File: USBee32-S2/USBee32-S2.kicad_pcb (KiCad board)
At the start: 4 copper layers, 28.1 x 68.3 mm, 50 parts, among them IC1 IP4220CZ6, J1 USB_A, J2 TYPE-C-31-M-12, J3 Conn_01x18_Male, J4 B2B-PH-SM4-TB(LF)(SN), J5 Conn_01x22_Male, Q1 MMBT8050, Q2 MMBT8050, SW1 SW_Push, SW2 SW_Push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

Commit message: Routing and placement cleaned
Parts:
- moved J4 15.1 mm to (171.5, 108.2), turned to 90 degrees
- moved R9 14.0 mm to (172.5, 97.7)
- moved R6 13.2 mm to (180.9, 114.2), turned to 0 degrees
- moved R8 13.0 mm to (172.5, 101.0), turned to 90 degrees
- moved SW2 12.6 mm to (169.2, 118.1)
- moved SW1 11.8 mm to (169.2, 122.0)
- moved C5 11.4 mm to (168.6, 113.6)
- moved C4 11.1 mm to (168.6, 115.4), turned to 0 degrees
- moved C1 10.2 mm to (179.1, 94.1), turned to 90 degrees
- moved R5 9.83 mm to (189.1, 102.7)
- moved Q2 9.75 mm to (186.1, 102.6)
- moved R7 9.23 mm to (175.7, 106.0), turned to 90 degrees
- moved R4 8.17 mm to (189.1, 98.8), turned to 90 degrees
- moved Q1 7.92 mm to (186.1, 98.8)
- moved R2 7.67 mm to (177.4, 94.1), turned to 270 degrees
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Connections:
- D4 pad 4: /GPIO_34 -> /GPIO_17
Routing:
- net /CHIP_PU: track 71.1 -> 94.6 mm, vias 2 -> 3
- net GND: track 69.7 -> 50.2 mm, vias 40 -> 42
- net /D1+: track 74.7 -> 56.6 mm, vias 1 -> 2
- net /GPIO_34: track 31.6 -> 18.7 mm, vias 2 -> 1
- net /GPIO_0: track 73.5 -> 84.0 mm, vias 2 -> 5
- net /VBUSC: track 29.6 -> 20.4 mm, vias 6 -> 0
- net /~RTS: track 6.76 -> 15.3 mm, vias 0 -> 2
- net /DN1: track 32.7 -> 25.3 mm, vias 3 -> 2
- net /DP1: track 32.7 -> 25.7 mm, vias 3 -> 2
- net /GPIO_8: track 59.4 -> 52.4 mm
- net /GPIO_17: track 39.2 -> 46.1 mm, vias 0 -> 3
- net +3V3: track 32.0 -> 26.0 mm, vias 9 -> 10
- net /CC2: track 7.99 -> 2.36 mm, vias 2 -> 0
- net Net-(C9-Pad1): track 10.5 -> 5.16 mm
- net +BATT: track 14.5 -> 10.6 mm
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
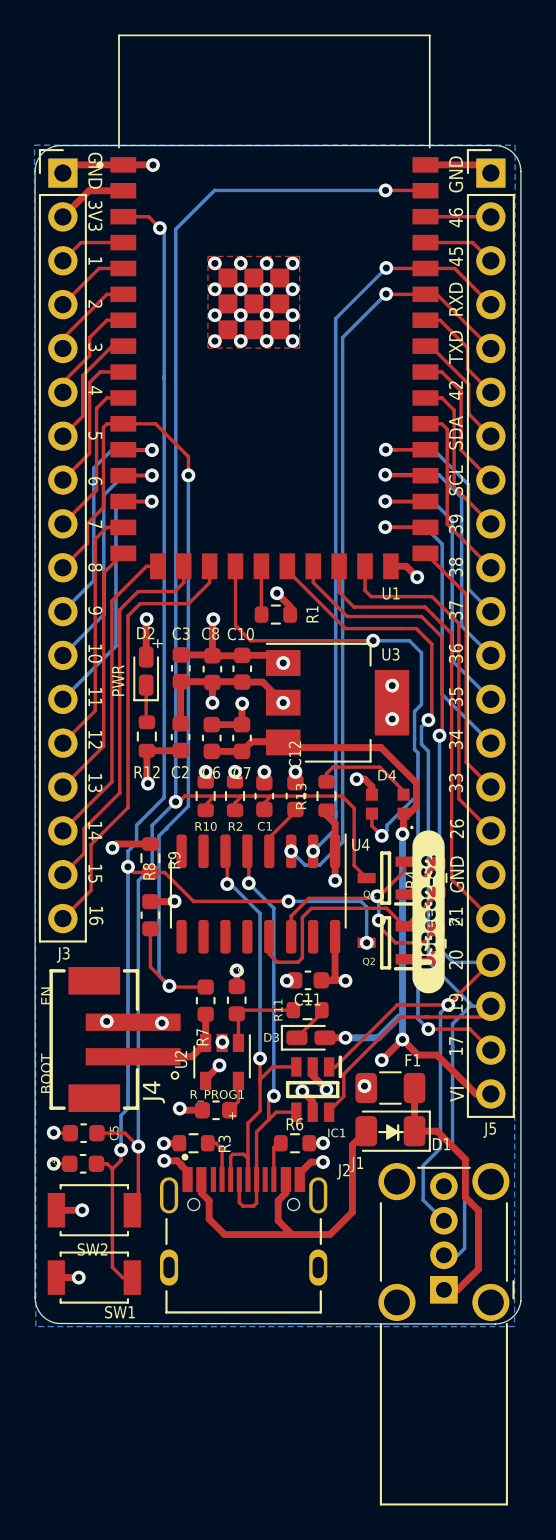
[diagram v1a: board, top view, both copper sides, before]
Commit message: Modified silkscreen
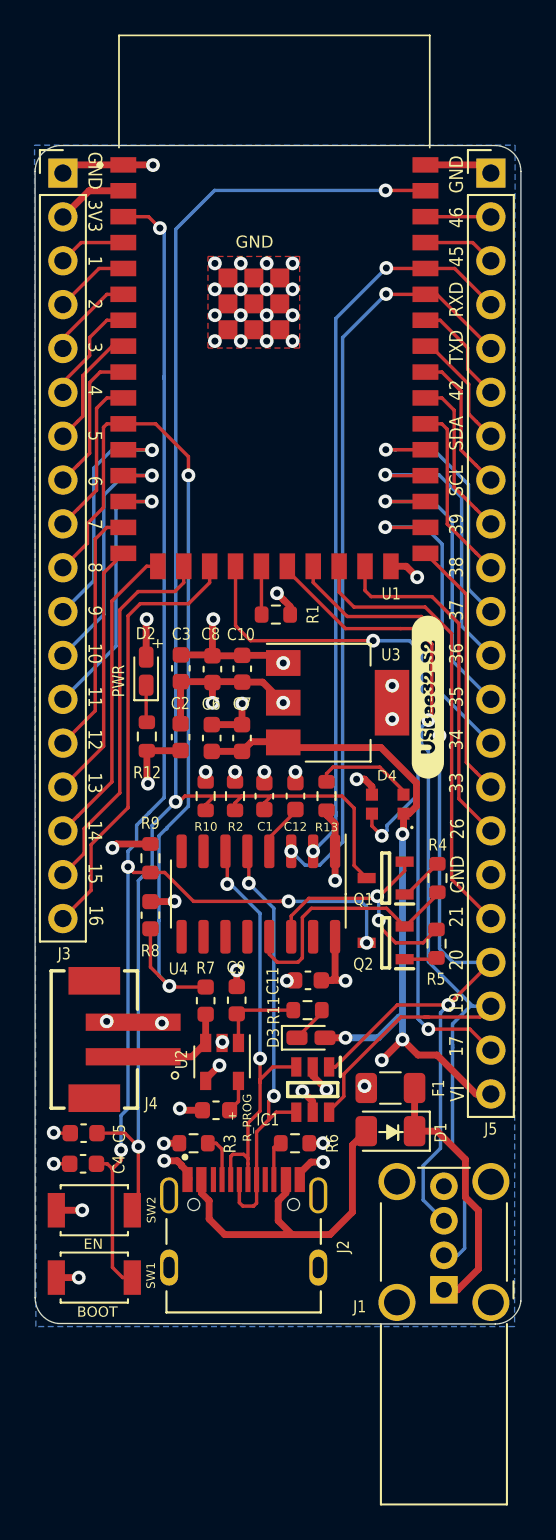
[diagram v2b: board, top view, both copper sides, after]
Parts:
- moved svg2mod 12.4 mm to (188.6, 88.4)
- renumbered R_PROG1 to R_PROG
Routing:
- added copper zone on B.Cu, net (none)
- removed copper zone on B.Cu, net GND

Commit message: Added differential pair to USB circuitry
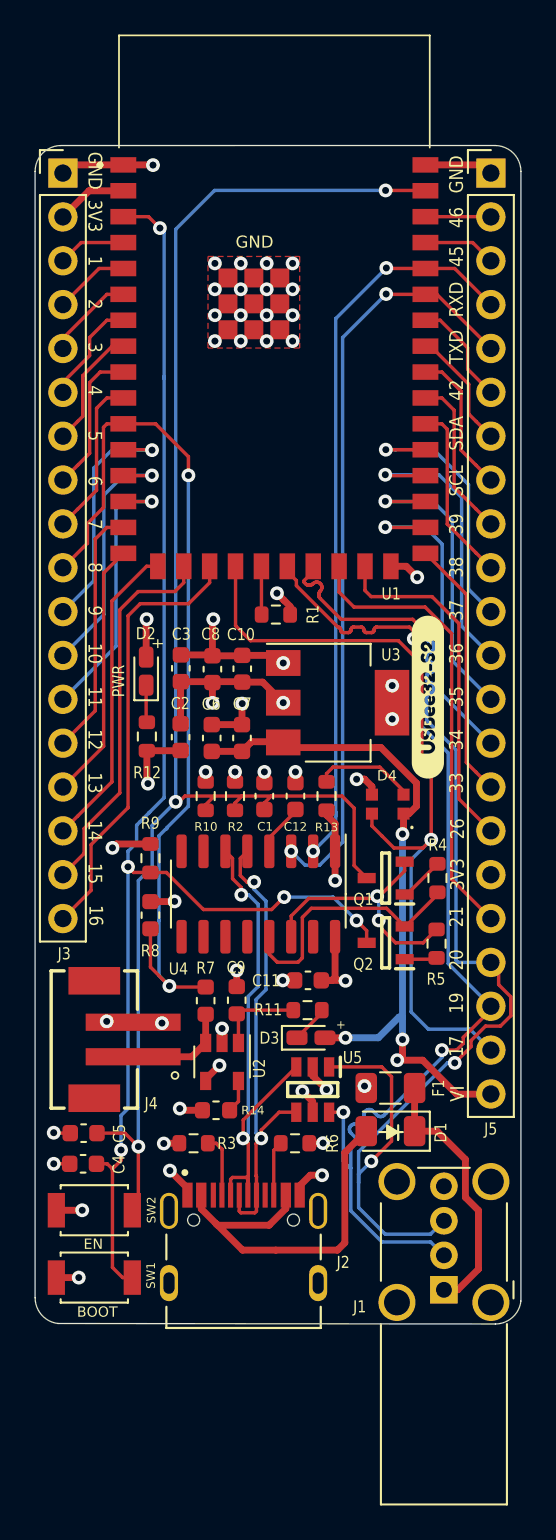
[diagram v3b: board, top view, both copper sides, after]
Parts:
- moved J2 0.90 mm to (177.9, 122.3)
- moved REF** 0.26 mm to (178.8, 59.7)
- renumbered R_PROG to R14, IC1 to U5
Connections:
- J5 pad 17: GND -> +3V3
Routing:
- net /D1+: track 56.6 -> 69.4 mm, vias 2 -> 3
- net /DN1: track 25.3 -> 29.8 mm
- net /VBUSC: track 20.4 -> 22.5 mm
- net /DP1: track 25.7 -> 27.3 mm
- net /CC1: track 2.72 -> 3.63 mm
- net /CC2: track 2.36 -> 3.17 mm
- net /VI: track 45.0 -> 44.2 mm
- net /GPIO_0: track 84.0 -> 83.2 mm
- net GND: track 50.2 -> 50.8 mm
- net /D1-: track 64.0 -> 63.5 mm, vias 1 -> 3
- net /GPIO_17: track 46.1 -> 46.4 mm, vias 3 -> 1
- removed copper zone on B.Cu, net (none)

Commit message: Updated silkscreen
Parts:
- removed the REF** at (179.1, 100.5)
- added G***: LOGO, USBee32-S2-Label:usbee32s2-qr, B.Cu at (179.7, 104.9)
- added REF**: KiCad-Logo_5mm_SilkScreen, Designs:KiCad-Logo_5mm_SilkScreen, B.Cu at (182.7, 59.7)
- moved REF** 5.54 mm to (173.3, 60.1)
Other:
- board text added: "DESIGNED WITH"
